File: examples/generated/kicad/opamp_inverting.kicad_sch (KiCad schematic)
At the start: 6 parts

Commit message: Attempt to create legible symbols.
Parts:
- RF, RIN: symbol examples:R -> R
- VCC, VEE, VIN: symbol examples:VSOURCE -> VSOURCE
- XU1: symbol examples:OPAMP -> OPAMP
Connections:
- net GND: now also VCC.1 (E1), VEE.1 (E1), VIN.2 (E2), XU1.2 (-)
- net VCC: now also VCC.2 (E2)
- new net: RF.2, RIN.2, XU1.1 (+)
- new net: RF.1, XU1.3
- new net: RIN.1, VIN.1 (E1)
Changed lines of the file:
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@@
     (comment 1 "Generated by mixedsig2cad")
   )
-  (symbol (lib_id "examples:VSOURCE") (at 45.00 40.00 0) (unit 1)
+  (symbol (lib_id "VSOURCE") (at 45.00 40.00 0) (unit 1)
     (in_bom yes) (on_board yes)
     (property "Reference" "VCC" (at 45.0 36.19 0)
@@
     )
   )
-  (symbol (lib_id "examples:VSOURCE") (at 45.00 120.00 0) (unit 1)
+  (symbol (lib_id "VSOURCE") (at 45.00 120.00 0) (unit 1)
     (in_bom yes) (on_board yes)
     (property "Reference" "VEE" (at 45.0 116.19 0)
@@
     )
   )
-  (symbol (lib_id "examples:VSOURCE") (at 45.00 80.00 90) (unit 1)
+  (symbol (lib_id "VSOURCE") (at 45.00 80.00 90) (unit 1)
     (in_bom yes) (on_board yes)
     (property "Reference" "VIN" (at 45.0 76.19 0)
@@
     )
   )
-  (symbol (lib_id "examples:R") (at 90.00 80.00 90) (unit 1)
+  (symbol (lib_id "R") (at 90.00 80.00 90) (unit 1)
     (in_bom yes) (on_board yes)
     (property "Reference" "RIN" (at 90.0 76.19 0)
@@
     )
   )
-  (symbol (lib_id "examples:R") (at 135.00 55.00 90) (unit 1)
+  (symbol (lib_id "R") (at 135.00 55.00 90) (unit 1)
     (in_bom yes) (on_board yes)
     (property "Reference" "RF" (at 135.0 51.19 0)
@@
     )
   )
-  (symbol (lib_id "examples:OPAMP") (at 145.00 80.00 0) (unit 1)
+  (symbol (lib_id "OPAMP") (at 145.00 80.00 0) (unit 1)
     (in_bom yes) (on_board yes)
     (property "Reference" "XU1" (at 145.0 76.19 0)
@@
     )
   )
-  (symbol (lib_id "examples:GND") (at 33.00 26.38 0) (unit 1)
+  (symbol (lib_id "GND") (at 33.00 26.38 0) (unit 1)
     (in_bom yes) (on_board yes)
     (property "Reference" "#PWR0001" (at 33.0 22.570000000000004 0)
@@
     )
   )
-  (symbol (lib_id "examples:VCC") (at 33.00 41.62 0) (unit 1)
+  (symbol (lib_id "VCC") (at 33.00 41.62 0) (unit 1)
     (in_bom yes) (on_board yes)
     (property "Reference" "#PWR0002" (at 33.0 37.809999999999995 0)

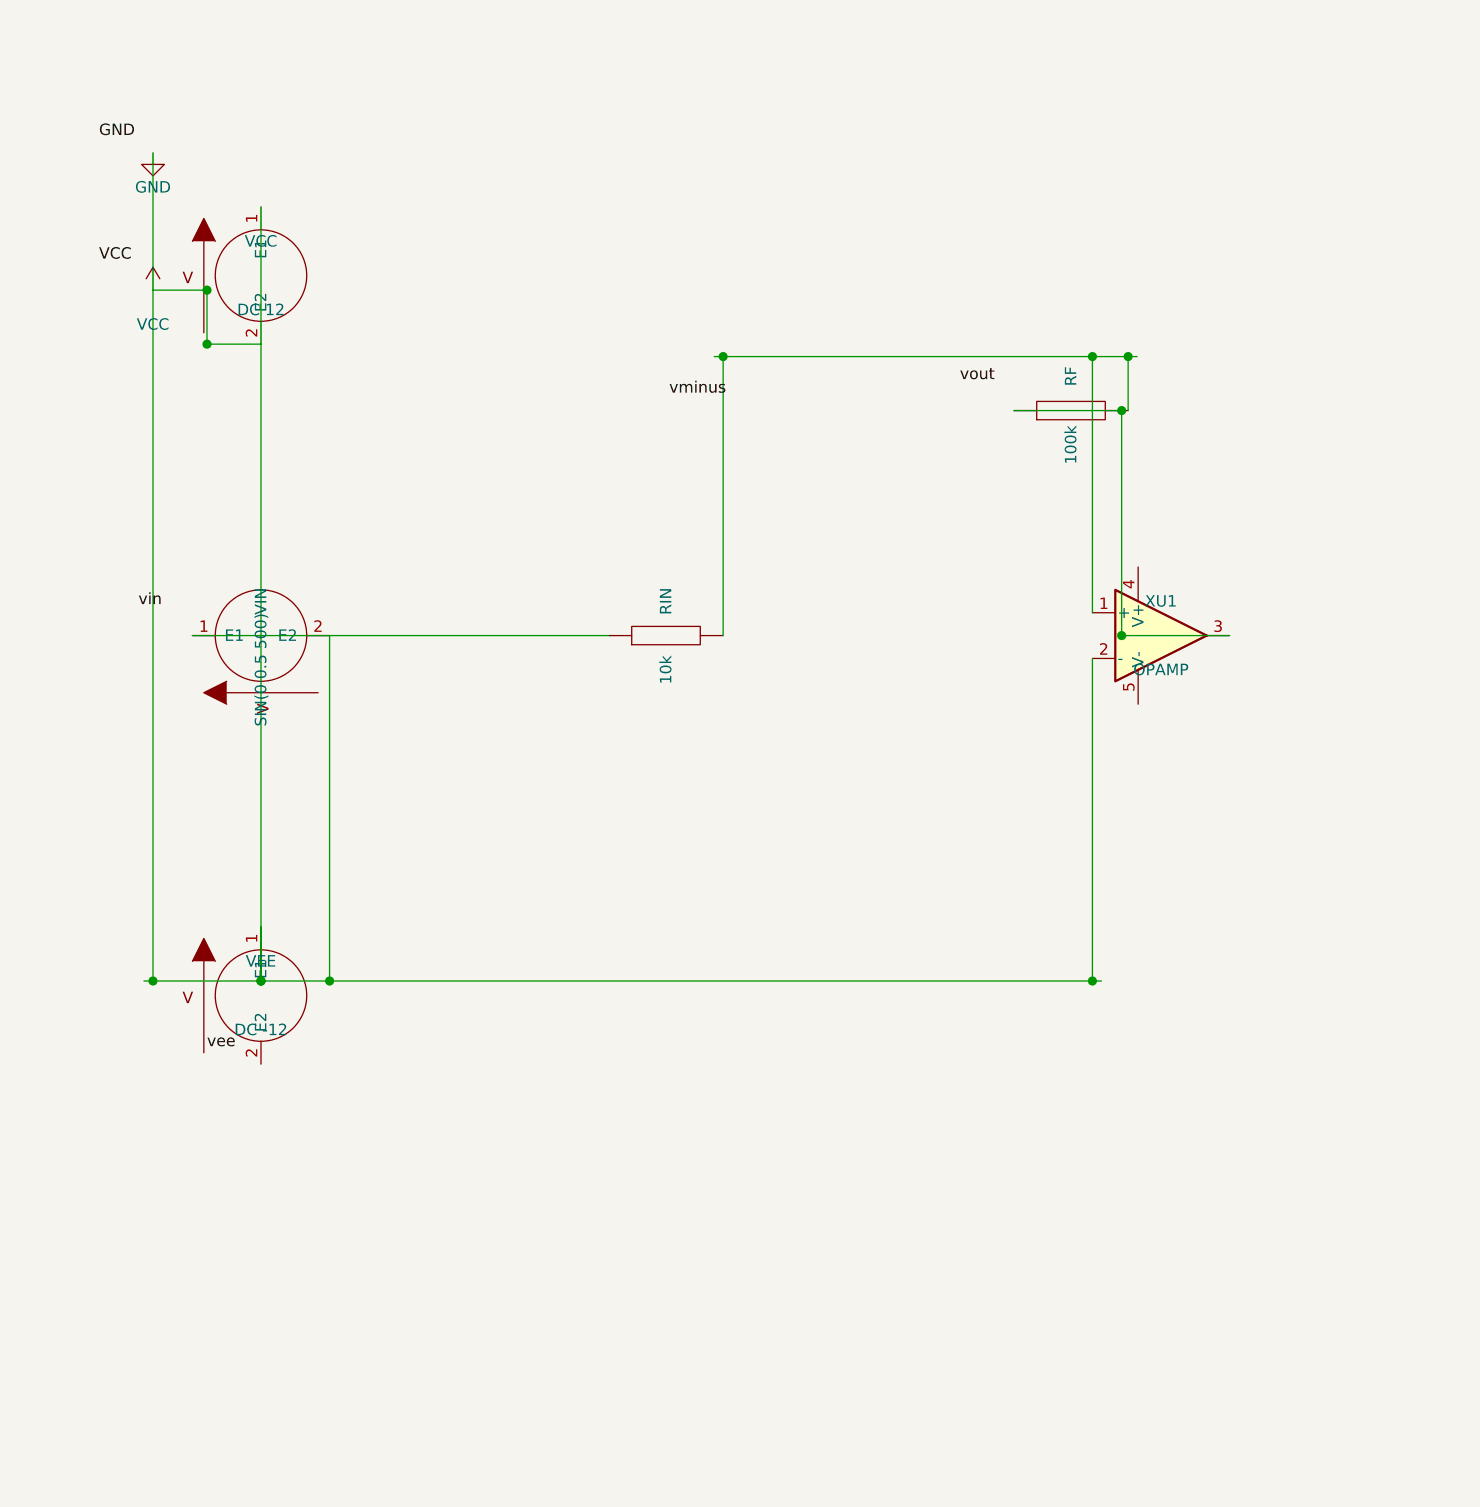
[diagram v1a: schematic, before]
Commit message: Attempt full seperation of circuit concerns into layers.
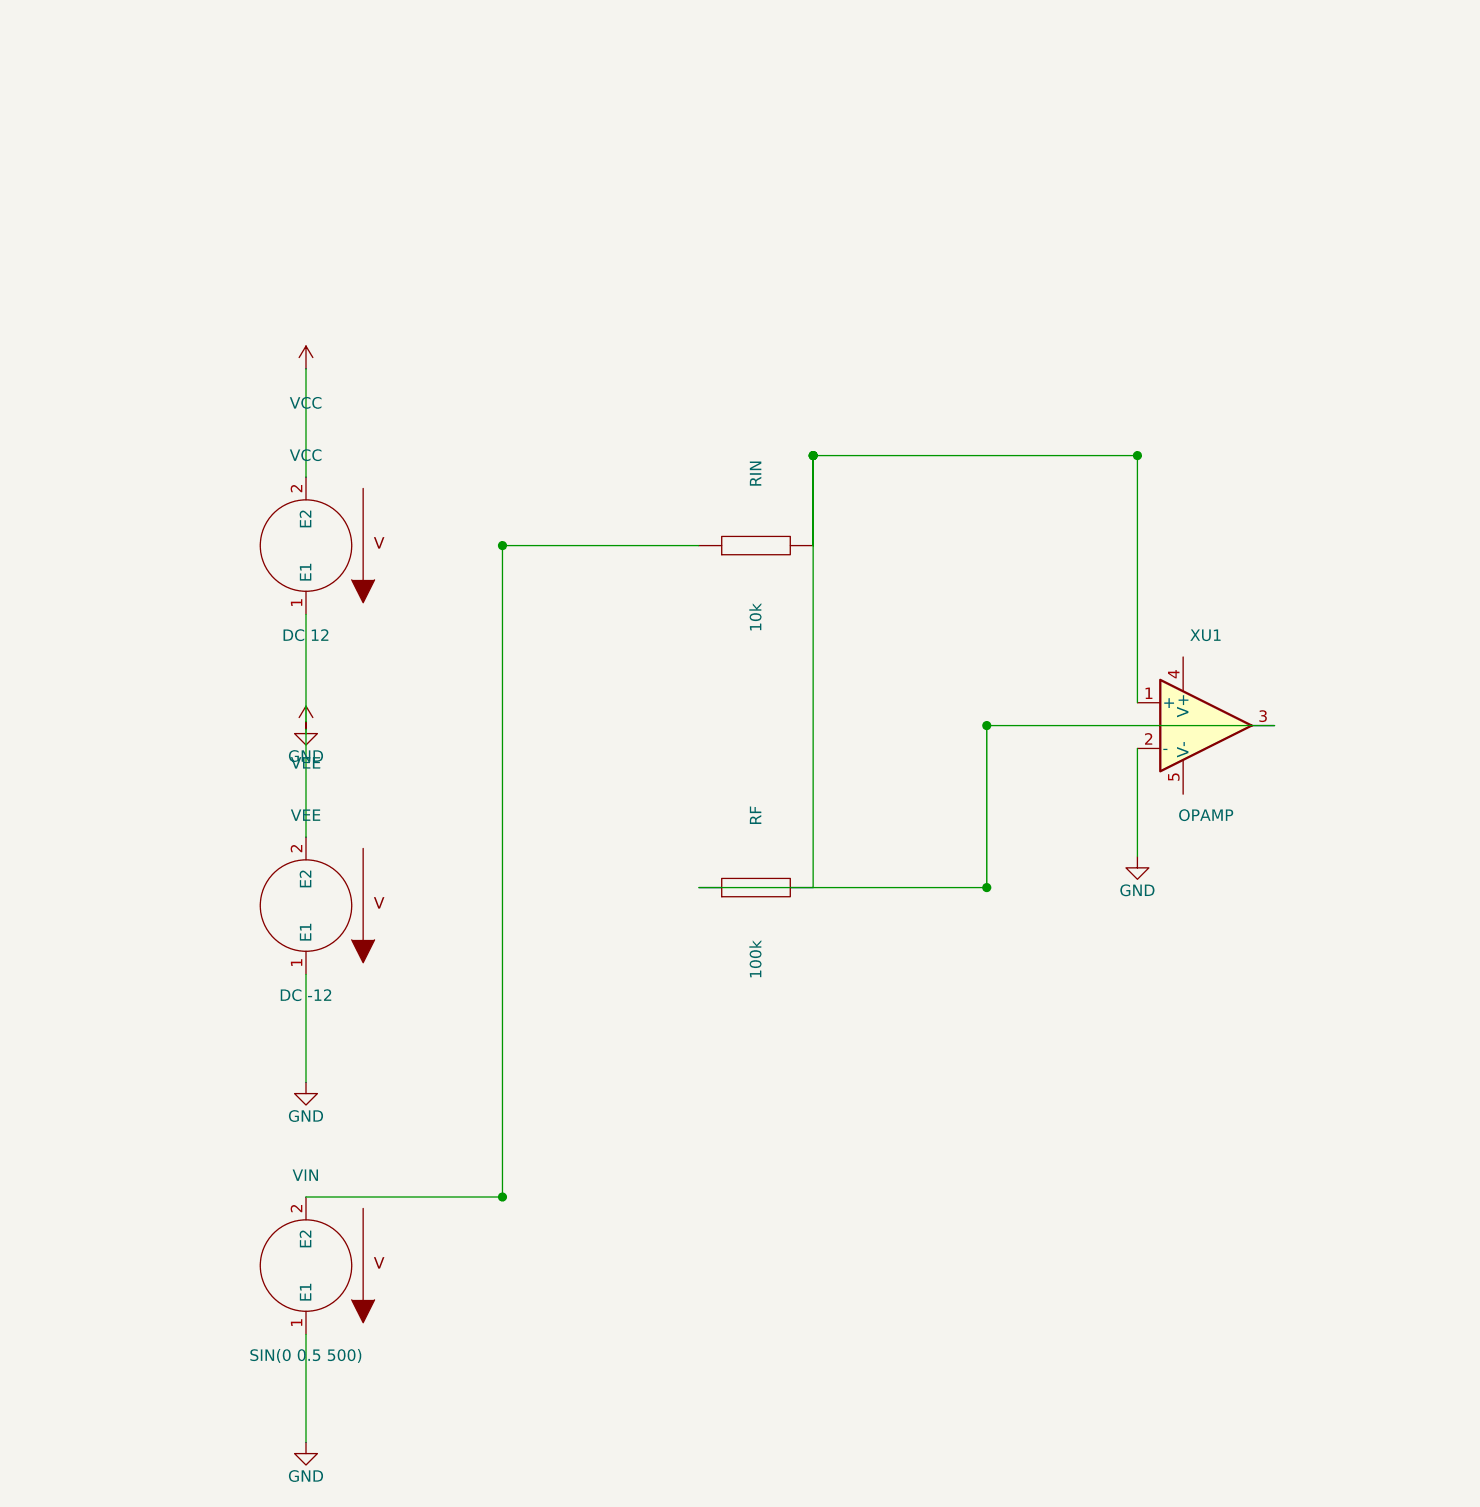
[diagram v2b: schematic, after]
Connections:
- net GND: now also VIN.1 (E1); no longer VIN.2 (E2)
- net at RIN.1: now also VIN.2 (E2); no longer VIN.1 (E1)
- net VEE: now reaches VEE.2 (E2)
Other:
- moved on the sheet: RF, RIN, VCC, VEE, VIN, XU1

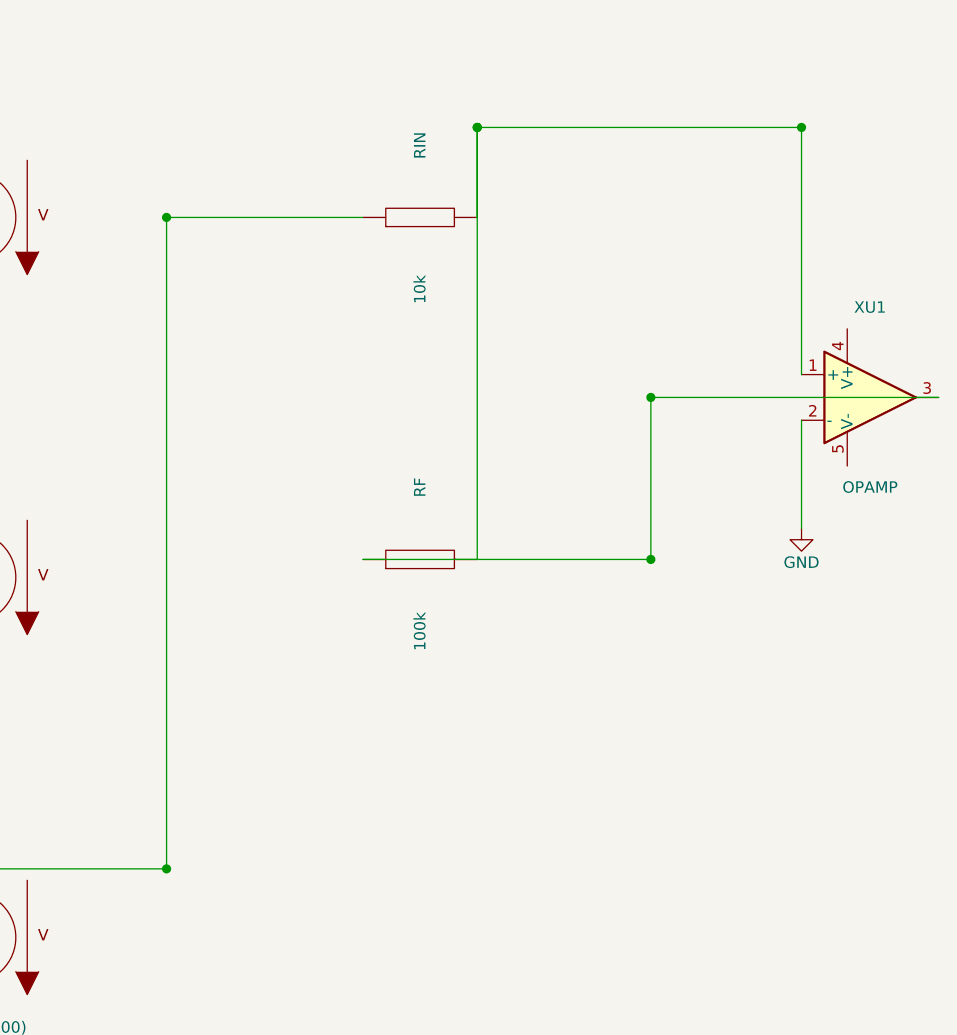
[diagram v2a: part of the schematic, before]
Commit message: Add checks for connectivity.
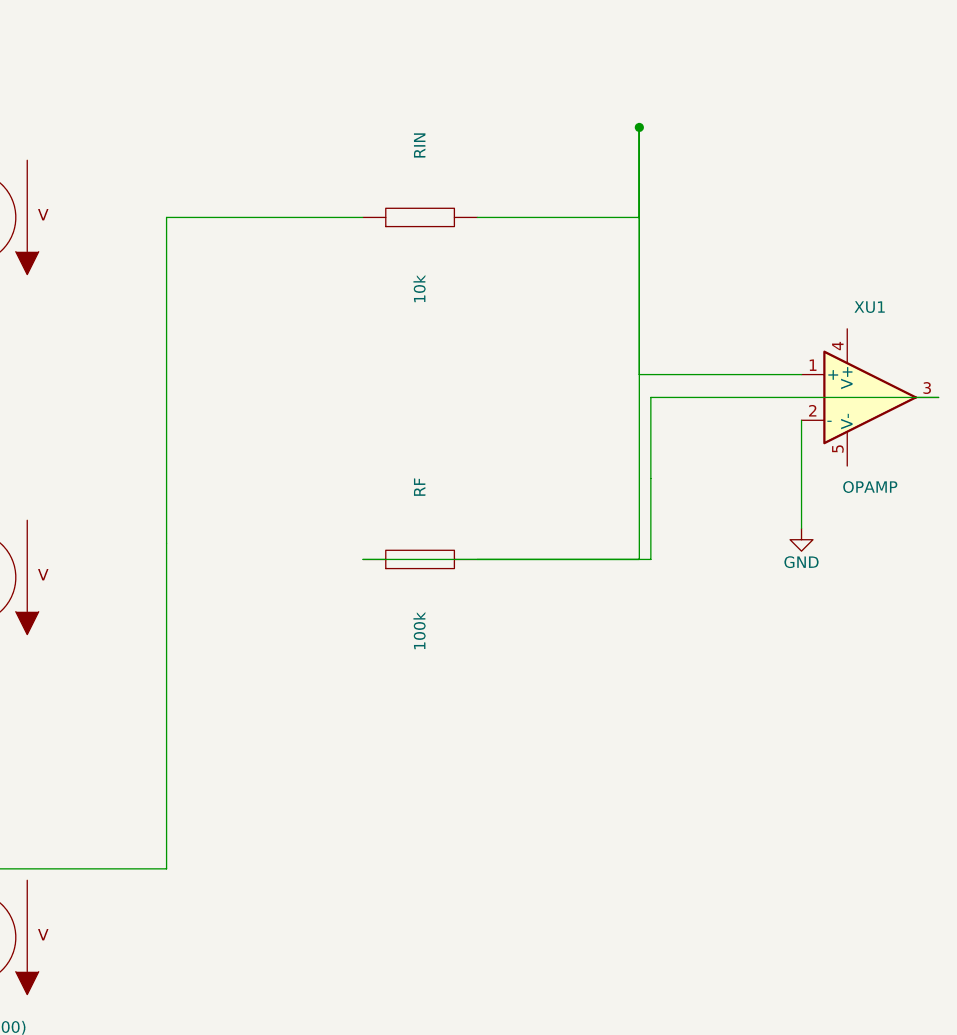
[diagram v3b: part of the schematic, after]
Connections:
- net at RF.2, RIN.2, XU1.1 (+): now also RF.1, XU1.3
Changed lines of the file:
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@@
     (stroke (width 0) (type solid) (color 0 0 0 0))
   )
-  (wire (pts (xy 71.83 142.38) (xy 71.83 70.00))
+  (wire (pts (xy 71.83 142.38) (xy 71.83 106.19))
     (stroke (width 0) (type solid) (color 0 0 0 0))
   )
-  (wire (pts (xy 71.83 70.00) (xy 93.65 70.00))
+  (wire (pts (xy 93.65 70.00) (xy 71.83 70.00))
     (stroke (width 0) (type solid) (color 0 0 0 0))
   )
-  (wire (pts (xy 106.35 60.00) (xy 142.38 60.00))
+  (wire (pts (xy 71.83 70.00) (xy 71.83 106.19))
     (stroke (width 0) (type solid) (color 0 0 0 0))
   )
-  (wire (pts (xy 106.35 70.00) (xy 106.35 60.00))
+  (wire (pts (xy 106.35 70.00) (xy 124.36 70.00))
     (stroke (width 0) (type solid) (color 0 0 0 0))
   )
-  (wire (pts (xy 106.35 108.00) (xy 106.35 60.00))
+  (wire (pts (xy 124.36 70.00) (xy 124.36 60.00))
     (stroke (width 0) (type solid) (color 0 0 0 0))
   )
-  (wire (pts (xy 142.38 87.46) (xy 142.38 60.00))
+  (wire (pts (xy 106.35 108.00) (xy 124.36 108.00))
+    (stroke (width 0) (type solid) (color 0 0 0 0))
+  )
+  (wire (pts (xy 124.36 108.00) (xy 124.36 60.00))
+    (stroke (width 0) (type solid) (color 0 0 0 0))
+  )
+  (wire (pts (xy 142.38 87.46) (xy 124.36 87.46))
+    (stroke (width 0) (type solid) (color 0 0 0 0))
+  )
+  (wire (pts (xy 124.36 87.46) (xy 124.36 60.00))
     (stroke (width 0) (type solid) (color 0 0 0 0))
   )
@@
     (stroke (width 0) (type solid) (color 0 0 0 0))
   )
-  (wire (pts (xy 125.64 108.00) (xy 125.64 90.00))
+  (wire (pts (xy 125.64 108.00) (xy 125.64 99.00))
     (stroke (width 0) (type solid) (color 0 0 0 0))
   )
-  (wire (pts (xy 125.64 90.00) (xy 157.62 90.00))
+  (wire (pts (xy 157.62 90.00) (xy 125.64 90.00))
     (stroke (width 0) (type solid) (color 0 0 0 0))
   )
-  (junction (at 71.83 142.38) (diameter 1.016) (color 0 0 0 0))
-  (junction (at 71.83 70.00) (diameter 1.016) (color 0 0 0 0))
-  (junction (at 106.35 60.00) (diameter 1.016) (color 0 0 0 0))
-  (junction (at 106.35 60.00) (diameter 1.016) (color 0 0 0 0))
-  (junction (at 142.38 60.00) (diameter 1.016) (color 0 0 0 0))
-  (junction (at 125.64 108.00) (diameter 1.016) (color 0 0 0 0))
-  (junction (at 125.64 90.00) (diameter 1.016) (color 0 0 0 0))
+  (wire (pts (xy 125.64 90.00) (xy 125.64 99.00))
+    (stroke (width 0) (type solid) (color 0 0 0 0))
+  )
+  (junction (at 124.36 60.00) (diameter 1.016) (color 0 0 0 0))
   (sheet_instances
     (path "/" (page "1"))

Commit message: Attempt to correct strange wiring.
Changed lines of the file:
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@@
     )
   )
-  (symbol (lib_id "VCC") (at 50.00 90.38 0) (unit 1)
+  (symbol (lib_id "VCC") (at 38.00 96.38 0) (unit 1)
     (in_bom yes) (on_board yes)
-    (property "Reference" "#PWR0003" (at 50.0 86.57 0)
+    (property "Reference" "#PWR0003" (at 38.0 92.57 0)
       (effects (font (size 1.27 1.27)) hide)
     )
-    (property "Value" "VEE" (at 50.0 94.19 0)
+    (property "Value" "VEE" (at 38.0 100.19 0)
       (effects (font (size 1.27 1.27)))
     )
@@
     (stroke (width 0) (type solid) (color 0 0 0 0))
   )
-  (wire (pts (xy 50.00 102.38) (xy 50.00 90.38))
+  (wire (pts (xy 50.00 102.38) (xy 50.00 96.38))
+    (stroke (width 0) (type solid) (color 0 0 0 0))
+  )
+  (wire (pts (xy 50.00 96.38) (xy 38.00 96.38))
     (stroke (width 0) (type solid) (color 0 0 0 0))
   )
@@
     (stroke (width 0) (type solid) (color 0 0 0 0))
   )
-  (wire (pts (xy 50.00 142.38) (xy 71.83 142.38))
+  (wire (pts (xy 50.00 142.38) (xy 50.00 140.50))
     (stroke (width 0) (type solid) (color 0 0 0 0))
   )
-  (wire (pts (xy 71.83 142.38) (xy 71.83 106.19))
+  (wire (pts (xy 50.00 140.50) (xy 91.50 140.50))
     (stroke (width 0) (type solid) (color 0 0 0 0))
   )
-  (wire (pts (xy 93.65 70.00) (xy 71.83 70.00))
+  (wire (pts (xy 91.50 140.50) (xy 91.50 70.00))
     (stroke (width 0) (type solid) (color 0 0 0 0))
   )
-  (wire (pts (xy 71.83 70.00) (xy 71.83 106.19))
+  (wire (pts (xy 91.50 70.00) (xy 93.65 70.00))
     (stroke (width 0) (type solid) (color 0 0 0 0))
   )
@@
     (stroke (width 0) (type solid) (color 0 0 0 0))
   )
-  (wire (pts (xy 124.36 70.00) (xy 124.36 60.00))
+  (wire (pts (xy 124.36 70.00) (xy 124.36 78.00))
     (stroke (width 0) (type solid) (color 0 0 0 0))
   )
@@
     (stroke (width 0) (type solid) (color 0 0 0 0))
   )
-  (wire (pts (xy 124.36 108.00) (xy 124.36 60.00))
+  (wire (pts (xy 124.36 108.00) (xy 124.36 78.00))
     (stroke (width 0) (type solid) (color 0 0 0 0))
   )
@@
     (stroke (width 0) (type solid) (color 0 0 0 0))
   )
-  (wire (pts (xy 124.36 87.46) (xy 124.36 60.00))
+  (wire (pts (xy 124.36 87.46) (xy 124.36 78.00))
     (stroke (width 0) (type solid) (color 0 0 0 0))
   )
-  (wire (pts (xy 93.65 108.00) (xy 125.64 108.00))
+  (wire (pts (xy 93.65 108.00) (xy 148.38 108.00))
     (stroke (width 0) (type solid) (color 0 0 0 0))
   )
-  (wire (pts (xy 125.64 108.00) (xy 125.64 99.00))
+  (wire (pts (xy 148.38 108.00) (xy 148.38 90.00))
     (stroke (width 0) (type solid) (color 0 0 0 0))
   )
-  (wire (pts (xy 157.62 90.00) (xy 125.64 90.00))
+  (wire (pts (xy 148.38 90.00) (xy 157.62 90.00))
     (stroke (width 0) (type solid) (color 0 0 0 0))
   )
-  (wire (pts (xy 125.64 90.00) (xy 125.64 99.00))
-    (stroke (width 0) (type solid) (color 0 0 0 0))
-  )
-  (junction (at 124.36 60.00) (diameter 1.016) (color 0 0 0 0))
+  (junction (at 124.36 78.00) (diameter 1.016) (color 0 0 0 0))
   (sheet_instances
     (path "/" (page "1"))

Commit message: Attempt shape and wiring fixes again.
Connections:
- net at RF.2, RIN.2, XU1.1 (+): no longer RF.1, XU1.3
- net at RIN.1, VIN.2 (E2): now also RF.1, XU1.3
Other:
- moved on the sheet: RF, RIN, VCC, VEE, VIN, XU1
